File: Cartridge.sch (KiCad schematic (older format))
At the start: 4 parts, among them J212 Diag, J24 Cartridge, J4 Expansion

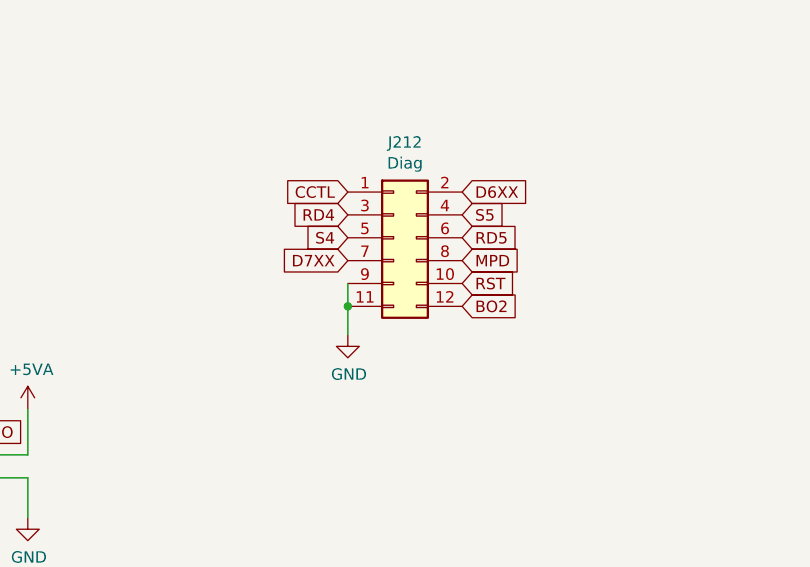
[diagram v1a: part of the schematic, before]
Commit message: Change THT on SMD
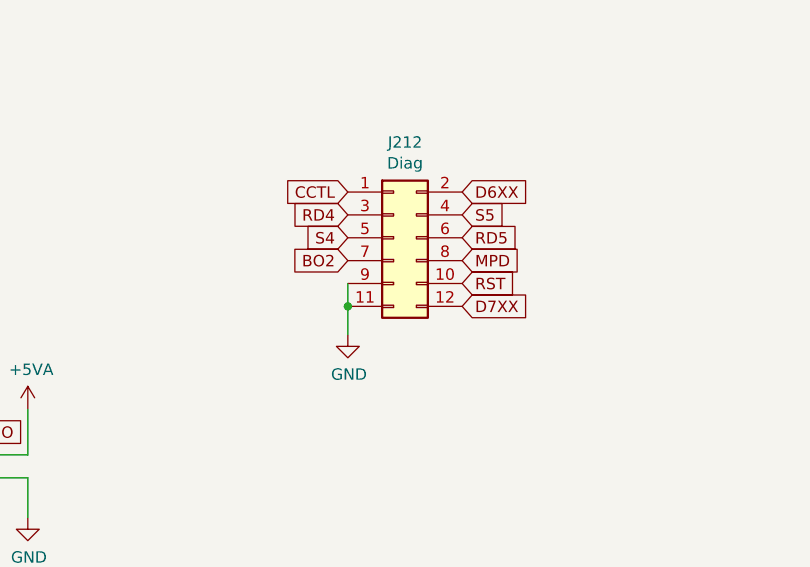
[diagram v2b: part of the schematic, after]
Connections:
- net BO2: now also J212.7 (Pin_7); no longer J212.12 (Pin_12)
- net D7XX: now also J212.12 (Pin_12); no longer J212.7 (Pin_7)
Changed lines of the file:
@@
 	1    0    0    -1
 $EndComp
+Text GLabel 5025 3300 2    50   Input ~ 0
+D7XX
 Text GLabel 4525 3100 0    50   Input ~ 0
-D7XX
-Text GLabel 5025 3300 2    50   Input ~ 0
 BO2
 Text GLabel 4525 2800 0    50   Input ~ 0

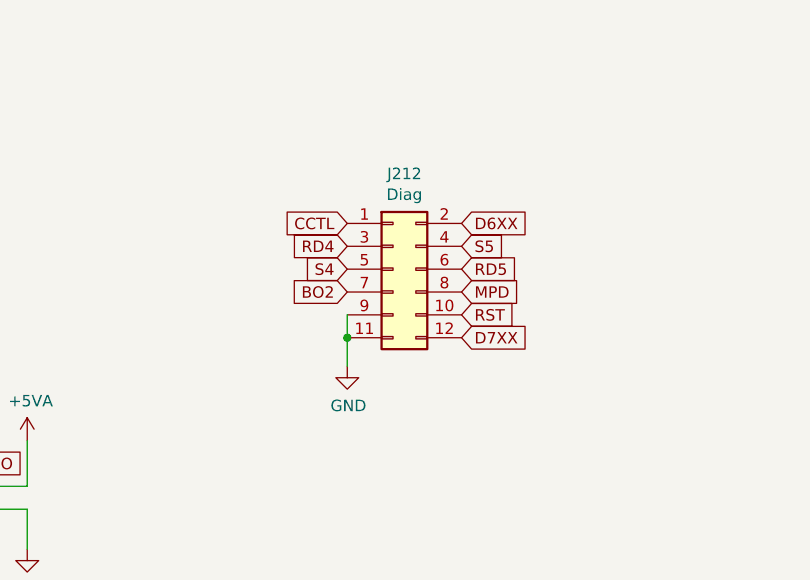
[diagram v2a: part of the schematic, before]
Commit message: OSS and Basic in PLCC
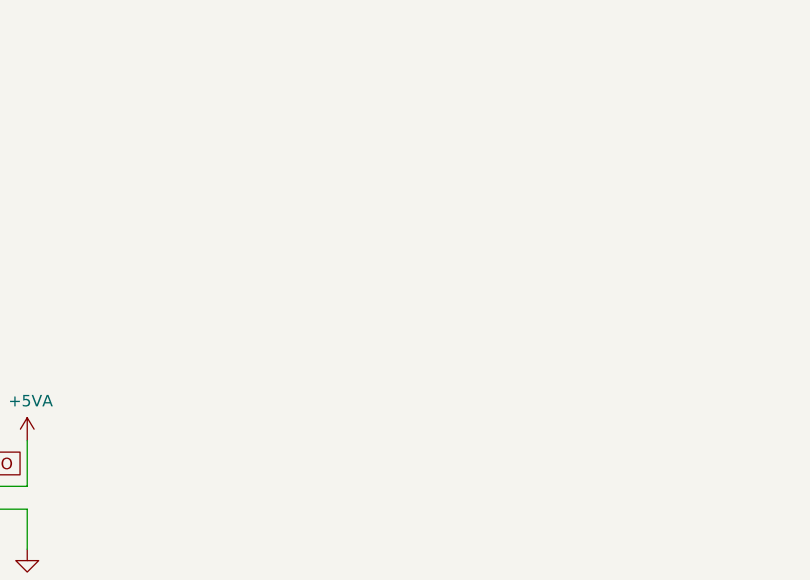
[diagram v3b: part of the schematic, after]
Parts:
- removed J212: Diag, Connector_PinHeader_2.54mm:PinHeader_2x06_P2.54mm_Vertical, symbol Connector_Generic:Conn_02x06_Odd_Even
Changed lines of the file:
@@
 	1    0    0    -1
 $EndComp
-Text GLabel 5025 3300 2    50   Input ~ 0
-D7XX
-Text GLabel 4525 3100 0    50   Input ~ 0
-BO2
-Text GLabel 4525 2800 0    50   Input ~ 0
-CCTL
-Text GLabel 4525 3000 0    50   Input ~ 0
-S4
-Text GLabel 4525 2900 0    50   Input ~ 0
-RD4
-Text GLabel 5025 2900 2    50   Input ~ 0
-S5
-Text GLabel 5025 3000 2    50   Input ~ 0
-RD5
-Text GLabel 5025 2800 2    50   Input ~ 0
-D6XX
-Text GLabel 5025 3200 2    50   Input ~ 0
-RST
-Text GLabel 5025 3100 2    50   Input ~ 0
-MPD
-$Comp
-L Connector_Generic:Conn_02x06_Odd_Even J212
-U 1 1 604B3554
-P 4725 3000
-F 0 "J212" H 4775 3417 50  0000 C CNN
-F 1 "Diag" H 4775 3326 50  0000 C CNN
-F 2 "Connector_PinHeader_2.54mm:PinHeader_2x06_P2.54mm_Vertical" H 4725 3000 50  0001 C CNN
-F 3 "~" H 4725 3000 50  0001 C CNN
-	1    4725 3000
-	1    0    0    -1
-$EndComp
-$Comp
-L power:GND #PWR0255
-U 1 1 604B4D92
-P 4525 3425
-F 0 "#PWR0255" H 4525 3175 50  0001 C CNN
-F 1 "GND" H 4530 3252 50  0000 C CNN
-F 2 "" H 4525 3425 50  0001 C CNN
-F 3 "" H 4525 3425 50  0001 C CNN
-	1    4525 3425
-	1    0    0    -1
-$EndComp
-Wire Wire Line
-	4525 3200 4525 3300
-Wire Wire Line
-	4525 3300 4525 3425
-Connection ~ 4525 3300
 $EndSCHEMATC

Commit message: Final modification
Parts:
- C18: footprint Atari:C_Axial_L5.1mm_D2.5mm_P12.50mm_Horizontal -> Capacitor_SMD:C_1206_3216Metric_Pad1.42x1.75mm_HandSolder
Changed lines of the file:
@@
 F 0 "C18" H 7590 5046 50  0000 L CNN
 F 1 "100nF" H 7590 4955 50  0000 L CNN
-F 2 "Atari:C_Axial_L5.1mm_D2.5mm_P12.50mm_Horizontal" H 7513 4850 50  0001 C CNN
+F 2 "Capacitor_SMD:C_1206_3216Metric_Pad1.42x1.75mm_HandSolder" H 7513 4850 50  0001 C CNN
 F 3 "~" H 7475 5000 50  0001 C CNN
 	1    7475 5000
